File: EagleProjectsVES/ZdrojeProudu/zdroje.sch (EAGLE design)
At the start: 30 parts, among them P1 COLLECTOR, P2 BASE, P3 EMITTER, P4 GROUND, P5 COL, P6 EMIT

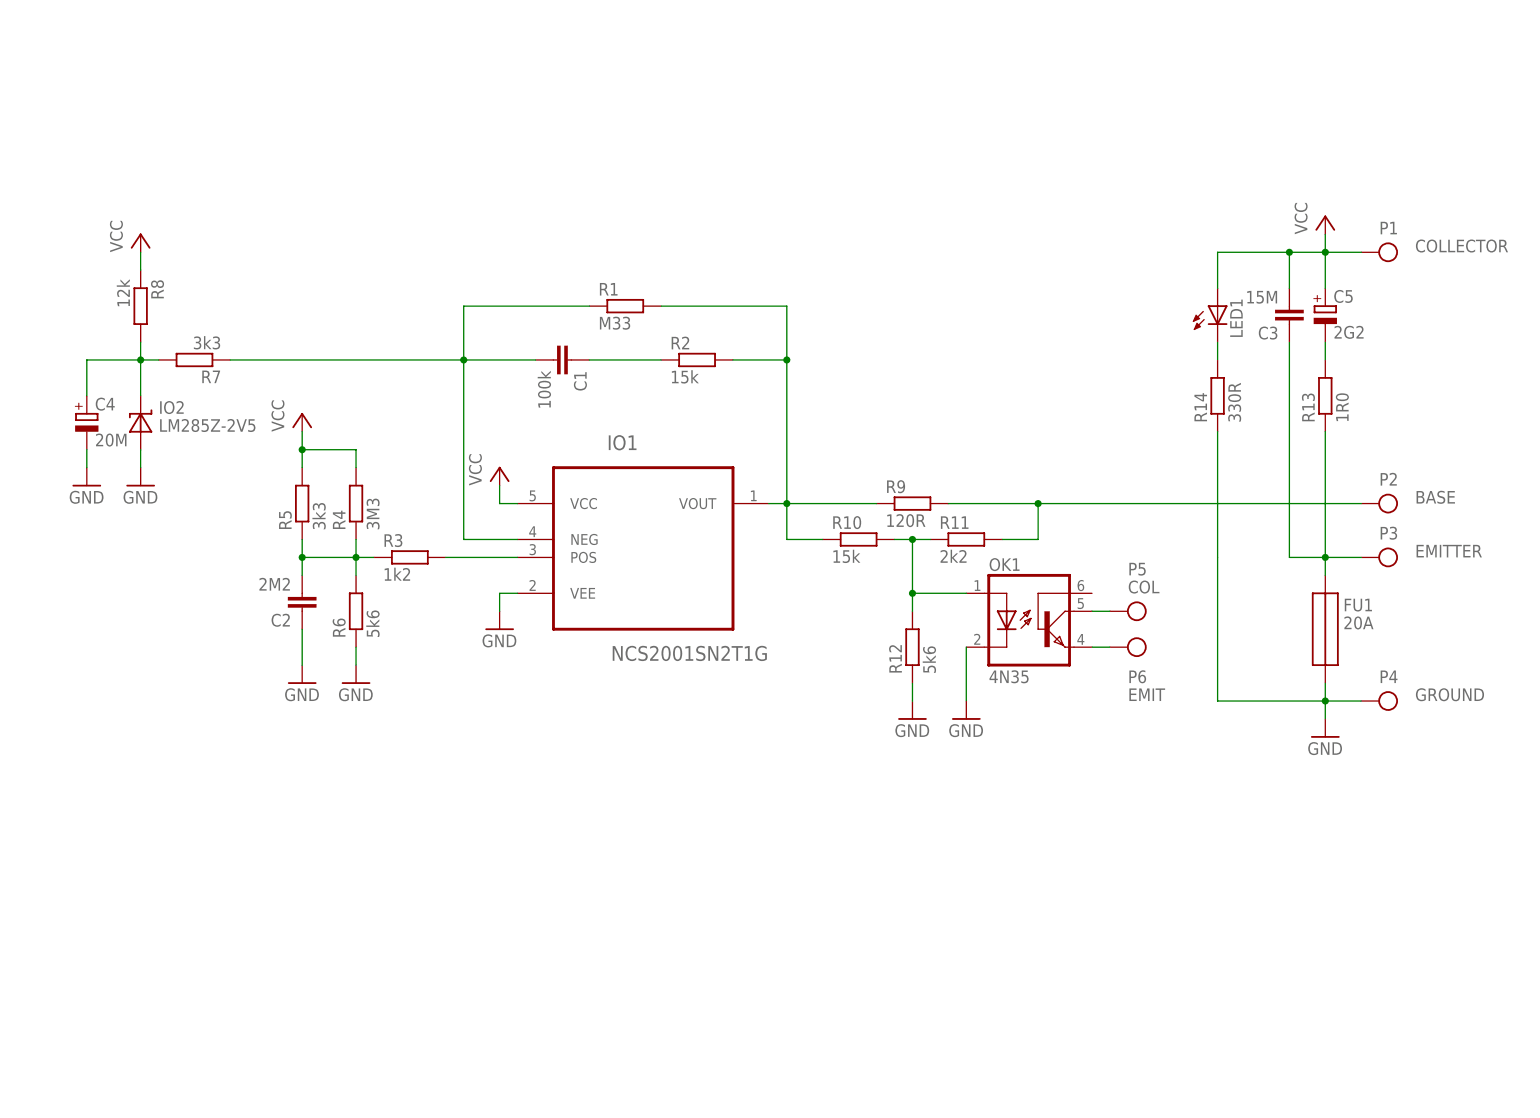
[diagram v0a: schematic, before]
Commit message: Eagle: - vybijec pro Papeze - tranzistory pred odeslanim do pragoboardu - navrh zdroju proudu
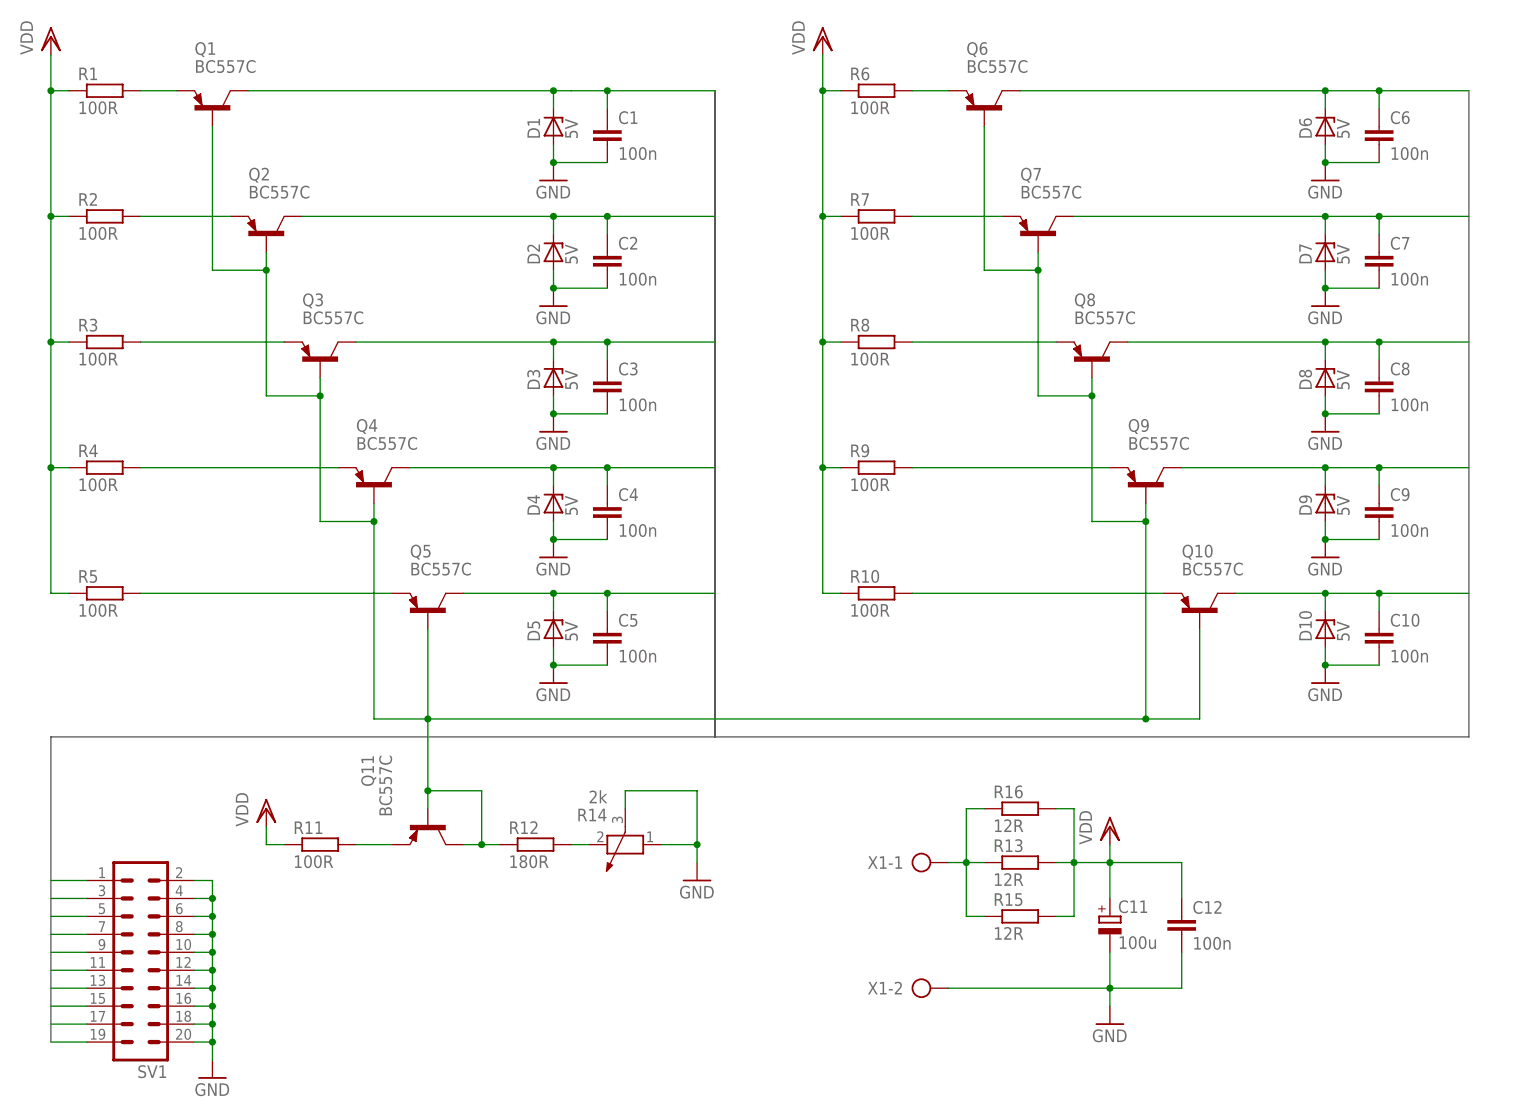
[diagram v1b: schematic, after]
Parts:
- removed FU1: 20A, pojistka:POJISTKA
- removed IO1: NCS2001SN2T1G, NCS2001:NCS2001SN2T1G
- removed IO2: LM285Z-2V5, LM285:LM285Z-2V5
- removed LED1: (no value), adafruit:LED3MM
- removed OK1: 4N35, optocoupler:4N35
- removed P1: COLLECTOR, PADs:PADPAD3MM
- removed P2: BASE, PADs:PADPAD3MM
- removed P3: EMITTER, PADs:PADPAD3MM
- removed P4: GROUND, PADs:PADPAD3MM
- removed P5: COL, PADs:PADPAD1.6MM
- removed P6: EMIT, PADs:PADPAD1.6MM
- added C10, C12, C6, C7, C8, C9: 100n, rcl:C-EU050-030X075
- added C11: 100u, rcl:CPOL-EUE5-8.5
- added D1, D10, D2, D3, D4, D5, D6, D7, D8, D9: 5V, diode:ZENER-DIODEDO35Z10
- added Q1, Q10, Q11, Q2, Q3, Q4, Q5, Q6, Q7, Q8, Q9: BC557C, transistor-pnp:BC557C
- added R15, R16: 12R, rcl:R-EU_0207/10
- added SV1: (no value), con-lstb:MA10-2
- added X1: (no value), con-ptr500:AK300/2
- C1: value 100k -> 100n; device rcl:C-EU050-025X075 -> rcl:C-EU050-030X075
- C2: value 2M2 -> 100n; device rcl:C-EU050-050X075 -> rcl:C-EU050-030X075
- C3: value 15M -> 100n; device rcl:C-EU050-075X075 -> rcl:C-EU050-030X075
- C4: value 20M -> 100n; device rcl:CPOL-EUE22-6AXIAL -> rcl:C-EU050-030X075
- C5: value 2G2 -> 100n; device rcl:CPOL-EUE5-10.5 -> rcl:C-EU050-030X075
- R1: value M33 -> 100R
- R10, R2: value 15k -> 100R
- R11: value 2k2 -> 100R
- R12: value 5k6 -> 180R
- R13: value 1R0 -> 12R; device rcl:R-EU_R1206 -> rcl:R-EU_0207/10
- R14: value 330R -> 2k; device rcl:R-EU_0207/10 -> rcl:POTENTIOMETER_PT_SPIN
- R3: value 1k2 -> 100R
- R4: value 3M3 -> 100R
- R5, R7: value 3k3 -> 100R
- R6: value 5k6 -> 100R
- R8: value 12k -> 100R
- R9: value 120R -> 100R
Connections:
- removed net VCC: C3.2, C5.+, IO1.VCC, LED1.A, P1.P$1, R4.2, R5.2, R8.1
- new net I1: C1.1, D1.C, Q1.C, SV1.1
- new net I10: C10.1, D10.C, Q10.C, SV1.19
- new net I2: C2.1, D2.C, Q2.C, SV1.3
- new net I3: C3.1, D3.C, Q3.C, SV1.5
- new net I4: C4.1, D4.C, Q4.C, SV1.7
- new net I5: C5.1, D5.C, Q5.C, SV1.9
- new net I6: C6.1, D6.C, Q6.C, SV1.11
- new net I7: C7.1, D7.C, Q7.C, SV1.13
- new net I8: C8.1, D8.C, Q8.C, SV1.15
- new net I9: C9.1, D9.C, Q9.C, SV1.17
- new net N$13: Q11.E, R11.2
- new net VDD: C11.+, C12.1, R1.1, R10.1, R11.1, R13.2, R15.2, R16.2, R2.1, R3.1, R4.1, R5.1, R6.1, R7.1, R8.1, R9.1
- net GND: now also C1.2, C10.2, C11.-, C12.2, C2.2, C3.2, C4.2, C5.2, C6.2, C7.2, C8.2, C9.2, D1.A, D10.A, D2.A, D3.A, D4.A, D5.A, D6.A, D7.A, D8.A, D9.A, R14.3, SV1.10, SV1.12, SV1.14, SV1.16, SV1.18, SV1.2, SV1.20, SV1.4, SV1.6, SV1.8, X1-2.KL; no longer C2.1, C4.-, FU1.P$2, IO1.VEE, IO2.ANODE, OK1.C, P4.P$1, R12.1, R6.1
- net N$1: now also Q1.E, R1.2; no longer C1.1, R2.1
- net N$10: now also Q10.E, R10.2; no longer OK1.COL, P5.P$1
- net N$11: now also R12.2, R14.2; no longer OK1.EMI, P6.P$1
- net N$12: now also Q1.B, Q10.B, Q11.B, Q11.C, Q2.B, Q3.B, Q4.B, Q5.B, Q6.B, Q7.B, Q8.B, Q9.B, R12.1; no longer LED1.C, R14.2
- net N$14: now also R13.1, R15.1, R16.1, X1-1.KL; no longer C5.-, R13.2
- net N$2: now also Q2.E; no longer IO1.VOUT, R1.2, R10.1, R9.1
- net N$3: now also Q3.E, R3.2; no longer C4.+, IO2.KATODE, R7.2, R8.2
- net N$4: now also Q4.E, R4.2; no longer C1.2, IO1.NEG, R1.1, R7.1
- net N$5: now also Q5.E, R5.2; no longer IO1.POS, R3.2
- net N$6: now also Q6.E; no longer C2.2, R3.1, R4.1, R5.1
- net N$7: now also Q7.E, R7.2; no longer C3.1, FU1.P$1, P3.P$1, R13.1
- net N$8: now also Q8.E, R8.2; no longer OK1.A, R10.2, R11.1, R12.2
- net N$9: now also Q9.E; no longer P2.P$1, R11.2
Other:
- moved on the sheet: C1, C2, C3, R1, R10, R11, R12, R13, R2, R3, R4, R5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
